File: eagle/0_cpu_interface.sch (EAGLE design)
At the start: 68 parts, among them IC1 74LS08N, IC10 74LS74N, IC11 74LS73N, IC12 MAX1232CPA, IC13 74LS32N, IC14 74LS244N, IC15 74LS74N, IC16 74LS14N, IC17 74LS541N, IC18 74LS541N, IC19 74LS541N, IC2 74LS541N, IC3 74LS245N, IC4 74LS245N, IC6 74LS541N, IC9 74LS74N

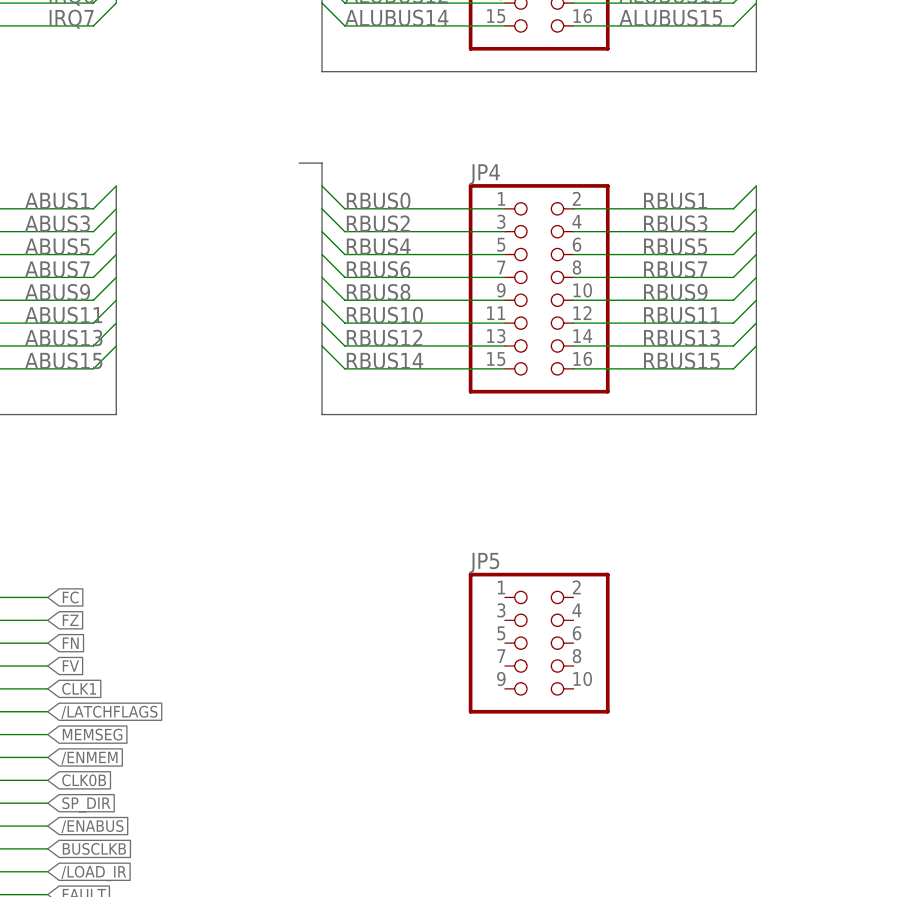
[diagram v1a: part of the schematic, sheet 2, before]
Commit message: Parts library updated (added fast SRAM), MMU board half complete
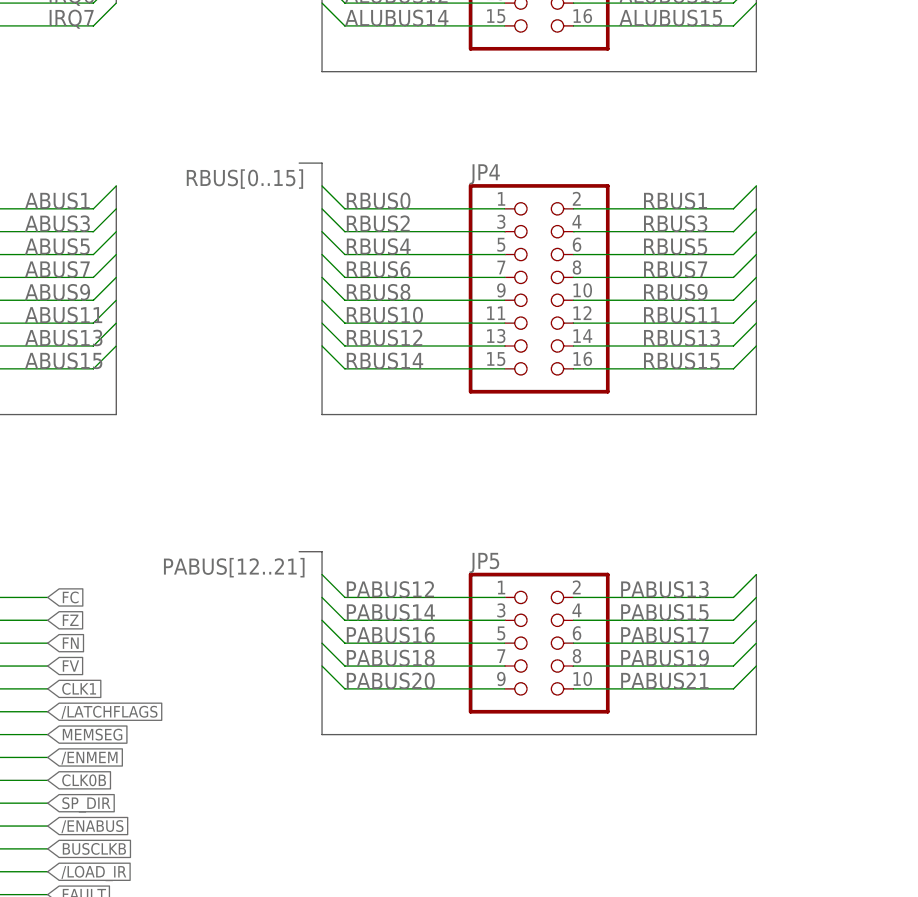
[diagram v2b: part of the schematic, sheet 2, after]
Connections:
- new net PABUS12: J1.C15, JP5.1
- new net PABUS13: J1.A15, JP5.2
- new net PABUS14: J1.C16, JP5.3
- new net PABUS15: J1.A16, JP5.4
- new net PABUS16: J1.C17, JP5.5
- new net PABUS17: J1.A17, JP5.6
- new net PABUS18: J1.C18, JP5.7
- new net PABUS19: J1.A18, JP5.8
- new net PABUS20: J1.C19, JP5.9
- new net PABUS21: J1.A19, JP5.10
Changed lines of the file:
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@@
 </segment>
 </bus>
+<bus name="PABUS[12..21]">
+<segment>
+<wire x1="132.08" y1="78.74" x2="134.62" y2="78.74" width="0.762" layer="92"/>
+<wire x1="134.62" y1="78.74" x2="134.62" y2="66.04" width="0.762" layer="92"/>
+</segment>
+<segment>
+<wire x1="187.96" y1="78.74" x2="190.5" y2="78.74" width="0.762" layer="92"/>
+<wire x1="190.5" y1="78.74" x2="190.5" y2="66.04" width="0.762" layer="92"/>
+</segment>
+</bus>
 </busses>
 <nets>
@@
 </segment>
 </net>
+<net name="PABUS12" class="0">
+<segment>
+<pinref part="J1" gate="G$1" pin="C15"/>
+<wire x1="190.5" y1="76.2" x2="187.96" y2="73.66" width="0.1524" layer="91"/>
+<wire x1="187.96" y1="73.66" x2="172.72" y2="73.66" width="0.1524" layer="91"/>
+<wire x1="170.18" y1="73.66" x2="172.72" y2="73.66" width="0.1524" layer="91"/>
+<label x="175.26" y="73.66" size="1.778" layer="95"/>
+</segment>
+</net>
+<net name="PABUS14" class="0">
+<segment>
+<pinref part="J1" gate="G$1" pin="C16"/>
+<wire x1="190.5" y1="73.66" x2="187.96" y2="71.12" width="0.1524" layer="91"/>
+<wire x1="187.96" y1="71.12" x2="170.18" y2="71.12" width="0.1524" layer="91"/>
+<label x="175.26" y="71.12" size="1.778" layer="95"/>
+</segment>
+</net>
+<net name="PABUS13" class="0">
+<segment>
+<pinref part="J1" gate="G$1" pin="A15"/>
+<wire x1="134.62" y1="76.2" x2="137.16" y2="73.66" width="0.1524" layer="91"/>
+<wire x1="137.16" y1="73.66" x2="149.86" y2="73.66" width="0.1524" layer="91"/>
+<label x="137.16" y="73.66" size="1.778" layer="95"/>
+</segment>
+</net>
+<net name="PABUS15" class="0">
+<segment>
+<pinref part="J1" gate="G$1" pin="A16"/>
+<wire x1="134.62" y1="73.66" x2="137.16" y2="71.12" width="0.1524" layer="91"/>
+<wire x1="137.16" y1="71.12" x2="149.86" y2="71.12" width="0.1524" layer="91"/>
+<label x="137.16" y="71.12" size="1.778" layer="95"/>
+</segment>
+</net>
+<net name="PABUS16" class="0">
+<segment>
+<pinref part="J1" gate="G$1" pin="C17"/>
+<wire x1="190.5" y1="71.12" x2="187.96" y2="68.58" width="0.1524" layer="91"/>
+<wire x1="187.96" y1="68.58" x2="170.18" y2="68.58" width="0.1524" layer="91"/>
+<label x="175.26" y="68.58" size="1.778" layer="95"/>
+</segment>
+</net>
+<net name="PABUS18" class="0">
+<segment>
+<pinref part="J1" gate="G$1" pin="C18"/>
+<wire x1="190.5" y1="68.58" x2="187.96" y2="66.04" width="0.1524" layer="91"/>
+<wire x1="187.96" y1="66.04" x2="170.18" y2="66.04" width="0.1524" layer="91"/>
+<label x="175.26" y="66.04" size="1.778" layer="95"/>
+</segment>
+</net>
+<net name="PABUS20" class="0">
+<segment>
+<pinref part="J1" gate="G$1" pin="C19"/>
+<wire x1="190.5" y1="66.04" x2="187.96" y2="63.5" width="0.1524" layer="91"/>
+<wire x1="187.96" y1="63.5" x2="170.18" y2="63.5" width="0.1524" layer="91"/>
+<label x="175.26" y="63.5" size="1.778" layer="95"/>
+</segment>
+</net>
+<net name="PABUS17" class="0">
+<segment>
+<pinref part="J1" gate="G$1" pin="A17"/>
+<wire x1="134.62" y1="71.12" x2="137.16" y2="68.58" width="0.1524" layer="91"/>
+<wire x1="137.16" y1="68.58" x2="149.86" y2="68.58" width="0.1524" layer="91"/>
+<label x="137.16" y="68.58" size="1.778" layer="95"/>
+</segment>
+</net>
+<net name="PABUS19" class="0">
+<segment>
+<pinref part="J1" gate="G$1" pin="A18"/>
+<wire x1="134.62" y1="68.58" x2="137.16" y2="66.04" width="0.1524" layer="91"/>
+<wire x1="137.16" y1="66.04" x2="149.86" y2="66.04" width="0.1524" layer="91"/>
+<label x="137.16" y="66.04" size="1.778" layer="95"/>
+</segment>
+</net>
+<net name="PABUS21" class="0">
+<segment>
+<pinref part="J1" gate="G$1" pin="A19"/>
+<wire x1="134.62" y1="66.04" x2="137.16" y2="63.5" width="0.1524" layer="91"/>
+<wire x1="137.16" y1="63.5" x2="149.86" y2="63.5" width="0.1524" layer="91"/>
+<label x="137.16" y="63.5" size="1.778" layer="95"/>
+</segment>
+</net>
 </nets>
 </sheet>
@@
 <wire x1="132.08" y1="172.72" x2="180.34" y2="172.72" width="0.762" layer="92"/>
 <wire x1="180.34" y1="172.72" x2="180.34" y2="198.12" width="0.762" layer="92"/>
+<label x="116.84" y="198.12" size="1.778" layer="95"/>
 </segment>
 </bus>
@@
 </segment>
 </bus>
+<bus name="PABUS[12..21]">
+<segment>
+<wire x1="129.54" y1="157.48" x2="132.08" y2="157.48" width="0.762" layer="92"/>
+<wire x1="132.08" y1="157.48" x2="132.08" y2="137.16" width="0.762" layer="92"/>
+<wire x1="132.08" y1="137.16" x2="180.34" y2="137.16" width="0.762" layer="92"/>
+<wire x1="180.34" y1="137.16" x2="180.34" y2="154.94" width="0.762" layer="92"/>
+<label x="114.3" y="154.94" size="1.778" layer="95"/>
+</segment>
+</bus>
 </busses>
 <nets>
@@
 </segment>
 </net>
+<net name="PABUS12" class="0">
+<segment>
+<pinref part="JP5" gate="A" pin="1"/>
+<wire x1="132.08" y1="154.94" x2="134.62" y2="152.4" width="0.1524" layer="91"/>
+<wire x1="134.62" y1="152.4" x2="152.4" y2="152.4" width="0.1524" layer="91"/>
+<label x="134.62" y="152.4" size="1.778" layer="95"/>
+</segment>
+</net>
+<net name="PABUS13" class="0">
+<segment>
+<pinref part="JP5" gate="A" pin="2"/>
+<wire x1="180.34" y1="154.94" x2="177.8" y2="152.4" width="0.1524" layer="91"/>
+<wire x1="177.8" y1="152.4" x2="160.02" y2="152.4" width="0.1524" layer="91"/>
+<label x="165.1" y="152.4" size="1.778" layer="95"/>
+</segment>
+</net>
+<net name="PABUS14" class="0">
+<segment>
+<pinref part="JP5" gate="A" pin="3"/>
+<wire x1="132.08" y1="152.4" x2="134.62" y2="149.86" width="0.1524" layer="91"/>
+<wire x1="134.62" y1="149.86" x2="152.4" y2="149.86" width="0.1524" layer="91"/>
+<label x="134.62" y="149.86" size="1.778" layer="95"/>
+</segment>
+</net>
+<net name="PABUS15" class="0">
+<segment>
+<pinref part="JP5" gate="A" pin="4"/>
+<wire x1="180.34" y1="152.4" x2="177.8" y2="149.86" width="0.1524" layer="91"/>
+<wire x1="177.8" y1="149.86" x2="160.02" y2="149.86" width="0.1524" layer="91"/>
+<label x="165.1" y="149.86" size="1.778" layer="95"/>
+</segment>
+</net>
+<net name="PABUS16" class="0">
+<segment>
+<pinref part="JP5" gate="A" pin="5"/>
+<wire x1="132.08" y1="149.86" x2="134.62" y2="147.32" width="0.1524" layer="91"/>
+<wire x1="134.62" y1="147.32" x2="152.4" y2="147.32" width="0.1524" layer="91"/>
+<label x="134.62" y="147.32" size="1.778" layer="95"/>
+</segment>
+</net>
+<net name="PABUS18" class="0">
+<segment>
+<pinref part="JP5" gate="A" pin="7"/>
+<wire x1="132.08" y1="147.32" x2="134.62" y2="144.78" width="0.1524" layer="91"/>
+<wire x1="134.62" y1="144.78" x2="152.4" y2="144.78" width="0.1524" layer="91"/>
+<label x="134.62" y="144.78" size="1.778" layer="95"/>
+</segment>
+</net>
+<net name="PABUS20" class="0">
+<segment>
+<pinref part="JP5" gate="A" pin="9"/>
+<wire x1="132.08" y1="144.78" x2="134.62" y2="142.24" width="0.1524" layer="91"/>
+<wire x1="134.62" y1="142.24" x2="152.4" y2="142.24" width="0.1524" layer="91"/>
+<label x="134.62" y="142.24" size="1.778" layer="95"/>
+</segment>
+</net>
+<net name="PABUS17" class="0">
+<segment>
+<pinref part="JP5" gate="A" pin="6"/>
+<wire x1="180.34" y1="149.86" x2="177.8" y2="147.32" width="0.1524" layer="91"/>
+<wire x1="177.8" y1="147.32" x2="160.02" y2="147.32" width="0.1524" layer="91"/>
+<label x="165.1" y="147.32" size="1.778" layer="95"/>
+</segment>
+</net>
+<net name="PABUS19" class="0">
+<segment>
+<pinref part="JP5" gate="A" pin="8"/>
+<wire x1="180.34" y1="147.32" x2="177.8" y2="144.78" width="0.1524" layer="91"/>
+<wire x1="177.8" y1="144.78" x2="160.02" y2="144.78" width="0.1524" layer="91"/>
+<label x="165.1" y="144.78" size="1.778" layer="95"/>
+</segment>
+</net>
+<net name="PABUS21" class="0">
+<segment>
+<pinref part="JP5" gate="A" pin="10"/>
+<wire x1="180.34" y1="144.78" x2="177.8" y2="142.24" width="0.1524" layer="91"/>
+<wire x1="177.8" y1="142.24" x2="160.02" y2="142.24" width="0.1524" layer="91"/>
+<label x="165.1" y="142.24" size="1.778" layer="95"/>
+</segment>
+</net>

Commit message: MMU schematics update
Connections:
- new net /ENMEMX: J1.C22
- new net /LDMEMX: J1.A22
- net /ENMEM: no longer J1.C22
- net /LDMEM: no longer J1.A22
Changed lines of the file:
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@@
-</segment>
-</net>
-<net name="/ENMEM" class="0">
-<segment>
-<pinref part="J1" gate="G$1" pin="C22"/>
-<wire x1="170.18" y1="55.88" x2="187.96" y2="55.88" width="0.1524" layer="91"/>
-<label x="187.96" y="55.88" size="1.4224" layer="95" xref="yes"/>
-</segment>
-</net>
-<net name="/LDMEM" class="0">
-<segment>
-<pinref part="J1" gate="G$1" pin="A22"/>
-<wire x1="149.86" y1="55.88" x2="137.16" y2="55.88" width="0.1524" layer="91"/>
-<label x="137.16" y="55.88" size="1.4224" layer="95" rot="R180" xref="yes"/>
 </segment>
 </net>
@@
 </segment>
 </net>
+<net name="/LDMEMX" class="0">
+<segment>
+<pinref part="J1" gate="G$1" pin="A22"/>
+<wire x1="149.86" y1="55.88" x2="137.16" y2="55.88" width="0.1524" layer="91"/>
+<label x="137.16" y="55.88" size="1.4224" layer="95" rot="R180" xref="yes"/>
+</segment>
+</net>
+<net name="/ENMEMX" class="0">
+<segment>
+<pinref part="J1" gate="G$1" pin="C22"/>
+<wire x1="170.18" y1="55.88" x2="187.96" y2="55.88" width="0.1524" layer="91"/>
+<label x="187.96" y="55.88" size="1.4224" layer="95" xref="yes"/>
+</segment>
+</net>

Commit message: More MMU changes, added PPREG
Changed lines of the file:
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@@
 <segment>
 <wire x1="129.54" y1="157.48" x2="132.08" y2="157.48" width="0.762" layer="92"/>
-<wire x1="132.08" y1="157.48" x2="132.08" y2="137.16" width="0.762" layer="92"/>
-<wire x1="132.08" y1="137.16" x2="180.34" y2="137.16" width="0.762" layer="92"/>
-<wire x1="180.34" y1="137.16" x2="180.34" y2="154.94" width="0.762" layer="92"/>
+<wire x1="132.08" y1="157.48" x2="132.08" y2="132.08" width="0.762" layer="92"/>
+<wire x1="132.08" y1="132.08" x2="180.34" y2="132.08" width="0.762" layer="92"/>
+<wire x1="180.34" y1="132.08" x2="180.34" y2="154.94" width="0.762" layer="92"/>
 <label x="114.3" y="154.94" size="1.778" layer="95"/>
 </segment>

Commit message: Removal of PPC started
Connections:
- removed net /LDPPC: JP10.11
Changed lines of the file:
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@@
-</segment>
-</net>
-<net name="/LDPPC" class="0">
-<segment>
-<wire x1="83.82" y1="139.7" x2="73.66" y2="139.7" width="0.1524" layer="91"/>
-<pinref part="JP10" gate="A" pin="11"/>
-<label x="73.66" y="139.7" size="1.27" layer="95" rot="R180" xref="yes"/>
 </segment>
 </net>

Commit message: Completed board 0
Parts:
- JP5: device pinhead:PINHD-2X5 -> pinhead:PINHD-2X6
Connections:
- new net /MEMOP: JP10.11
- net /ENMEMX: now also JP5.11
- net /FS: no longer J1.A11
- net /LDMEMX: now also JP5.12
- net MEMSEG: no longer J1.A21
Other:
- note added: "(C) 2010-2016"
- note removed: "(C) 2010-2014"
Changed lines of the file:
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@@
 <part name="SUPPLY25" library="supply2" deviceset="+5V" device=""/>
 <part name="SUPPLY33" library="supply2" deviceset="GND" device=""/>
-<part name="JP5" library="pinhead" deviceset="PINHD-2X5" device=""/>
+<part name="JP5" library="pinhead" deviceset="PINHD-2X6" device=""/>
 </parts>
 <sheets>
@@
 <text x="289.56" y="27.94" size="2.54" layer="97" font="vector">Clocks, reset, bus interface</text>
 <text x="386.08" y="33.02" size="2.54" layer="97" font="vector" rot="R180">Dawid Pilawa</text>
-<text x="386.08" y="27.94" size="2.54" layer="97" font="vector" rot="R180">(C) 2010-2014</text>
+<text x="386.08" y="27.94" size="2.54" layer="97" font="vector" rot="R180">(C) 2010-2016</text>
 <text x="370.84" y="10.16" size="2.54" layer="97" font="vector" rot="R180">CPU.0</text>
 <text x="386.08" y="10.16" size="2.54" layer="97" font="vector" rot="R180">2.0</text>
@@
 </segment>
 </net>
-<net name="/FS" class="0">
-<segment>
-<pinref part="J1" gate="G$1" pin="A11"/>
-<wire x1="149.86" y1="83.82" x2="134.62" y2="83.82" width="0.1524" layer="91"/>
-<label x="134.62" y="83.82" size="1.4224" layer="95" rot="R180" xref="yes"/>
-</segment>
-</net>
-<net name="MEMSEG" class="0">
-<segment>
-<pinref part="J1" gate="G$1" pin="A21"/>
-<wire x1="149.86" y1="58.42" x2="137.16" y2="58.42" width="0.1524" layer="91"/>
-<label x="137.16" y="58.42" size="1.4224" layer="95" rot="R180" xref="yes"/>
-</segment>
-</net>
 <net name="CLK0D" class="0">
 <segment>
@@
 <text x="289.56" y="27.94" size="2.54" layer="97" font="vector">Clocks, reset, bus interface</text>
 <text x="386.08" y="33.02" size="2.54" layer="97" font="vector" rot="R180">Dawid Pilawa</text>
-<text x="386.08" y="27.94" size="2.54" layer="97" font="vector" rot="R180">(C) 2010-2014</text>
+<text x="386.08" y="27.94" size="2.54" layer="97" font="vector" rot="R180">(C) 2010-2016</text>
 <text x="370.84" y="10.16" size="2.54" layer="97" font="vector" rot="R180">CPU.0</text>
 <text x="386.08" y="10.16" size="2.54" layer="97" font="vector" rot="R180">2.0</text>
@@
 </segment>
 </net>
+<net name="/ENMEMX" class="0">
+<segment>
+<pinref part="JP5" gate="A" pin="11"/>
+<wire x1="152.4" y1="139.7" x2="147.32" y2="139.7" width="0.1524" layer="91"/>
+<label x="147.32" y="139.7" size="1.4224" layer="95" rot="R180" xref="yes"/>
+</segment>
+</net>
+<net name="/LDMEMX" class="0">
+<segment>
+<pinref part="JP5" gate="A" pin="12"/>
+<wire x1="160.02" y1="139.7" x2="165.1" y2="139.7" width="0.1524" layer="91"/>
+<label x="165.1" y="139.7" size="1.4224" layer="95" xref="yes"/>
+</segment>
+</net>
+<net name="/MEMOP" class="0">
+<segment>
+<pinref part="JP10" gate="A" pin="11"/>
+<wire x1="83.82" y1="139.7" x2="73.66" y2="139.7" width="0.1524" layer="91"/>
+<label x="73.66" y="139.7" size="1.27" layer="95" rot="R180" xref="yes"/>
+</segment>
+</net>
